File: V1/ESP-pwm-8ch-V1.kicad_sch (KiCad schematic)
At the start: 47 parts, among them J1 12VDC, J2 CH1/2, J3 CH3/4, J4 CH5/6, J5 CH7/8, Q1 IRLB8721PBF, Q2 IRLB8721PBF, Q3 IRLB8721PBF, Q4 IRLB8721PBF, Q5 IRLB8721PBF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

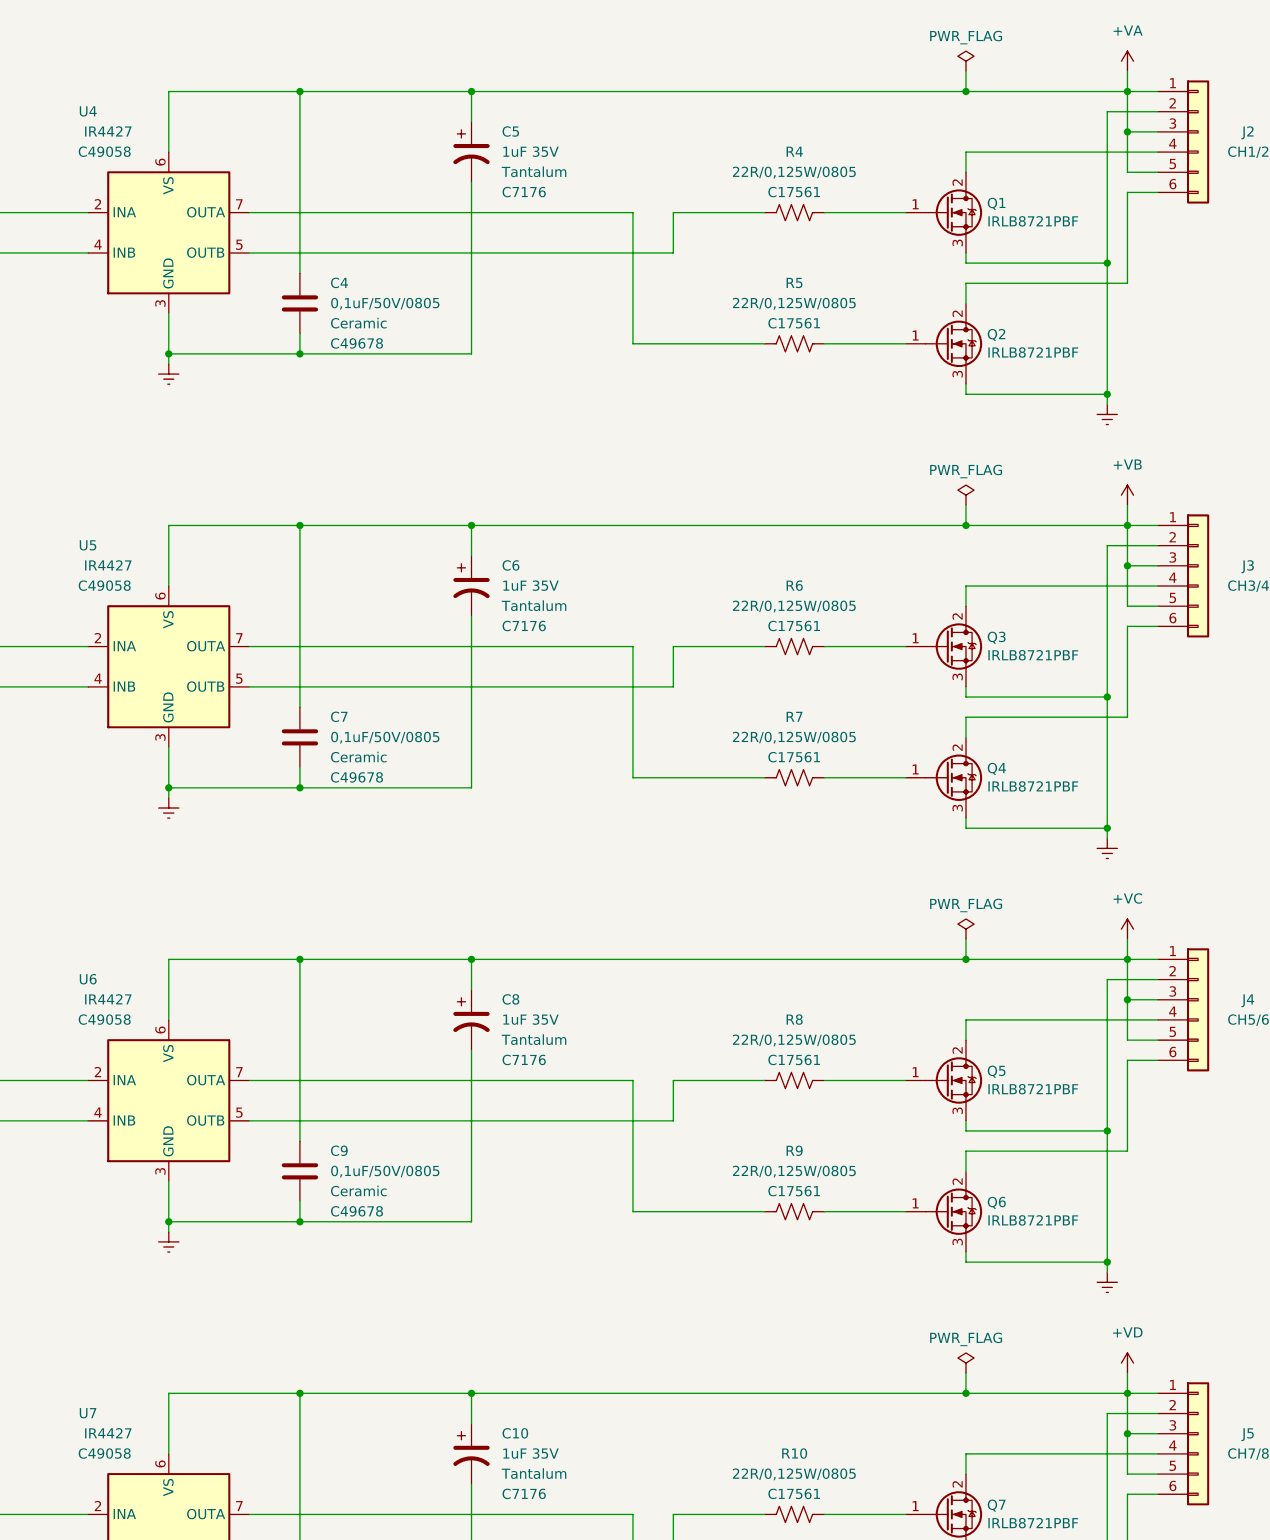
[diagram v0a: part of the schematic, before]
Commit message: Separated driver power lines from loads
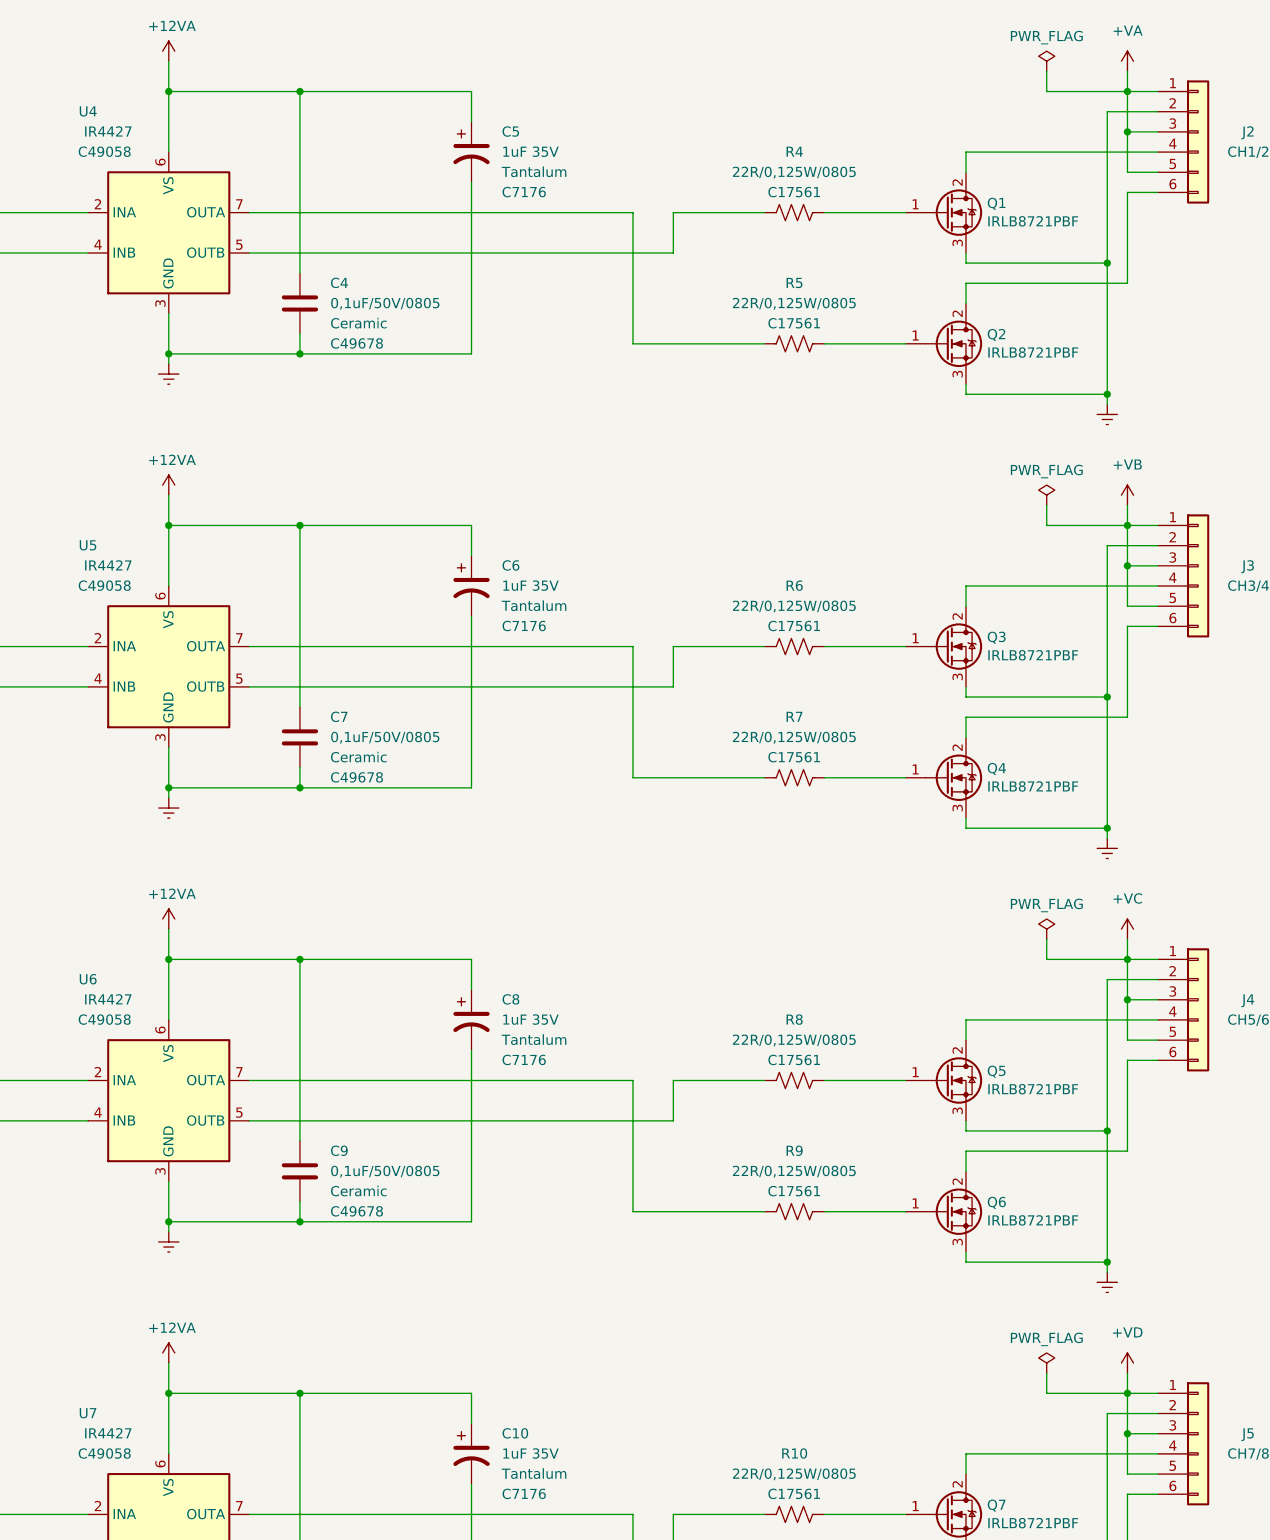
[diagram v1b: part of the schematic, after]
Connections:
- net +12VA: now also C10.1, C11.1, C4.1, C5.1, C6.1, C7.1, C8.1, C9.1, U4.6 (VS), U5.6 (VS), U6.6 (VS), U7.6 (VS)
- net +VA: no longer C4.1, C5.1, U4.6 (VS)
- net +VB: no longer C6.1, C7.1, U5.6 (VS)
- net +VC: no longer C8.1, C9.1, U6.6 (VS)
- net +VD: no longer C10.1, C11.1, U7.6 (VS)

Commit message: updated connectors
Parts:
- U2: footprint Tales:WEMOS_D1_mini_light_pads -> Module:WEMOS_D1_mini_light
- U3: footprint Tales:Olimex_ESP32-POE_Pads -> Tales:Olimex_ESP32-POE
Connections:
- net +3V3 renamed +3.3V
